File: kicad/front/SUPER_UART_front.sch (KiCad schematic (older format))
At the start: 0 parts

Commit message: Working on schematic
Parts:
- added MECH1: case, dummy, symbol dummy_mech
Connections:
- wire segments 0 -> 58
- no-connect marks 0 -> 4
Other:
- note added: "&"
- note added: "CS"
- note added: "CTS"
- note added: "DTR"
- note added: "FTDI PIN\n\nRxD\nTxD\nCTS\nRTS"
- note added: "FTDI PIN\n\nRxD\nTxD\nRTS"
- note added: "Function\n\nMOSI\nSCK\nCS\nMISO"
- note added: "Function\n\nSDA_OUT\nSCL\nSDA_IN"
- note added: "I2C connections"
- note added: "I2C mode"
- note added: "MISO"
- note added: "MOSI"
- note added: "Opto channel\n\nDTR\nTxD\nCTS"
- note added: "Opto channel\n\nDTR\nTxD\nRTS\nCTS"
- note added: "Output pin\n\nCTS\nTxD\nCTS"
- note added: "Output pin\n\nRxD\nTxD\nRTS\nCTS"
- note added: "RTS"
- note added: "RxD"
- note added: "RxD B\n\nTxD B"
- note added: "RxD C\n\nTxD C"
- note added: "RxD D"
- note added: "RxD D\n\nTxD D"
- note added: "SCK"
- note added: "SCL"
- note added: "SDA"
- note added: "SPI connections"
- note added: "SPI mode"
- note added: "SPY mode"
- note added: "TxD"
- note added: "TxD B"
- note added: "TxD C"
- note added: "TxD D"
- note added: "UART mode"
- note added: "WP"
- note added: "normal mode"

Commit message: Working on schematic
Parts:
- added C1: 10u, niceRLC:0805_N, symbol C
- added CON1: PIN-2x20, PIN-2x20_N, symbol PIN-2x20
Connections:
- net labels added: +5V, CLPD_OE, CPLD_BOOT_EN, CTS_A, CTS_B, CTS_C, CTS_D, DCD_D, DSR_D, DTR_A, DTR_B, DTR_C, DTR_D, EECLK, EECS, EEDATA, FTDI_RESET, GND, RI_D, RTS_D, RXD_A, RXD_B, RXD_C, RXD_D, SR_CLK, SR_DATA, SR_LOAD, TXD_A, TXD_B, TXD_C, TXD_D, ~CTS_A_OC, ~CTS_B_OC, ~PWREN, ~RXD_A_OC, ~RXD_B_OC, ~USB_SUSPEND
- wire segments 58 -> 178
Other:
- moved on the sheet: MECH1

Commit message: PCB placement
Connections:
- wire segments 178 -> 182
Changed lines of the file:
@@
 I2C connections
 $Sheet
-S 7100 850  1500 900
+S 7100 850  1500 1000
 U 5933A622
 F0 "SUPER_UART_front_RS232" 56
@@
 F16 "RXD_D3" I R 8600 1650 56
 F17 "TXD_D" I L 7100 1650 56
+F18 "~VDD1_EN" I R 8600 1750 56
 $EndSheet
 $Sheet
@@
 F4 "RXD_D_LED" I R 10850 3500 56
 F5 "DTR_B" I L 9200 2250 56
-F6 "TXD_D" I L 9200 1900 56
+F6 "TXD_D" I L 9200 1650 56
 F7 "DTR_D1" I L 9200 1150 56
 F8 "RTS_D1" I L 9200 1050 56
@@
 	9200 4550 8600 4550
 Wire Wire Line
-	7000 1900 9200 1900
-Wire Wire Line
 	8600 2800 8700 2800
 Wire Wire Line
-	8700 2800 8700 1900
-Connection ~ 8700 1900
+	8700 2800 8700 1950
+Connection ~ 8700 1950
 Wire Wire Line
 	8600 2900 8800 2900
@@
 	3250 4250 3950 4250
 Wire Wire Line
-	7000 1900 7000 1650
+	7000 1650 7000 1950
 Connection ~ 7000 1650
 Wire Wire Line
@@
 Wire Wire Line
 	2100 5850 2100 5800
+Wire Wire Line
+	7000 1950 9000 1950
+Wire Wire Line
+	9000 1950 9000 1650
+Wire Wire Line
+	9000 1650 9200 1650
+Wire Wire Line
+	8600 1750 8900 1750
+Wire Wire Line
+	8900 1750 8900 3300
+Connection ~ 8900 3300
 $EndSCHEMATC

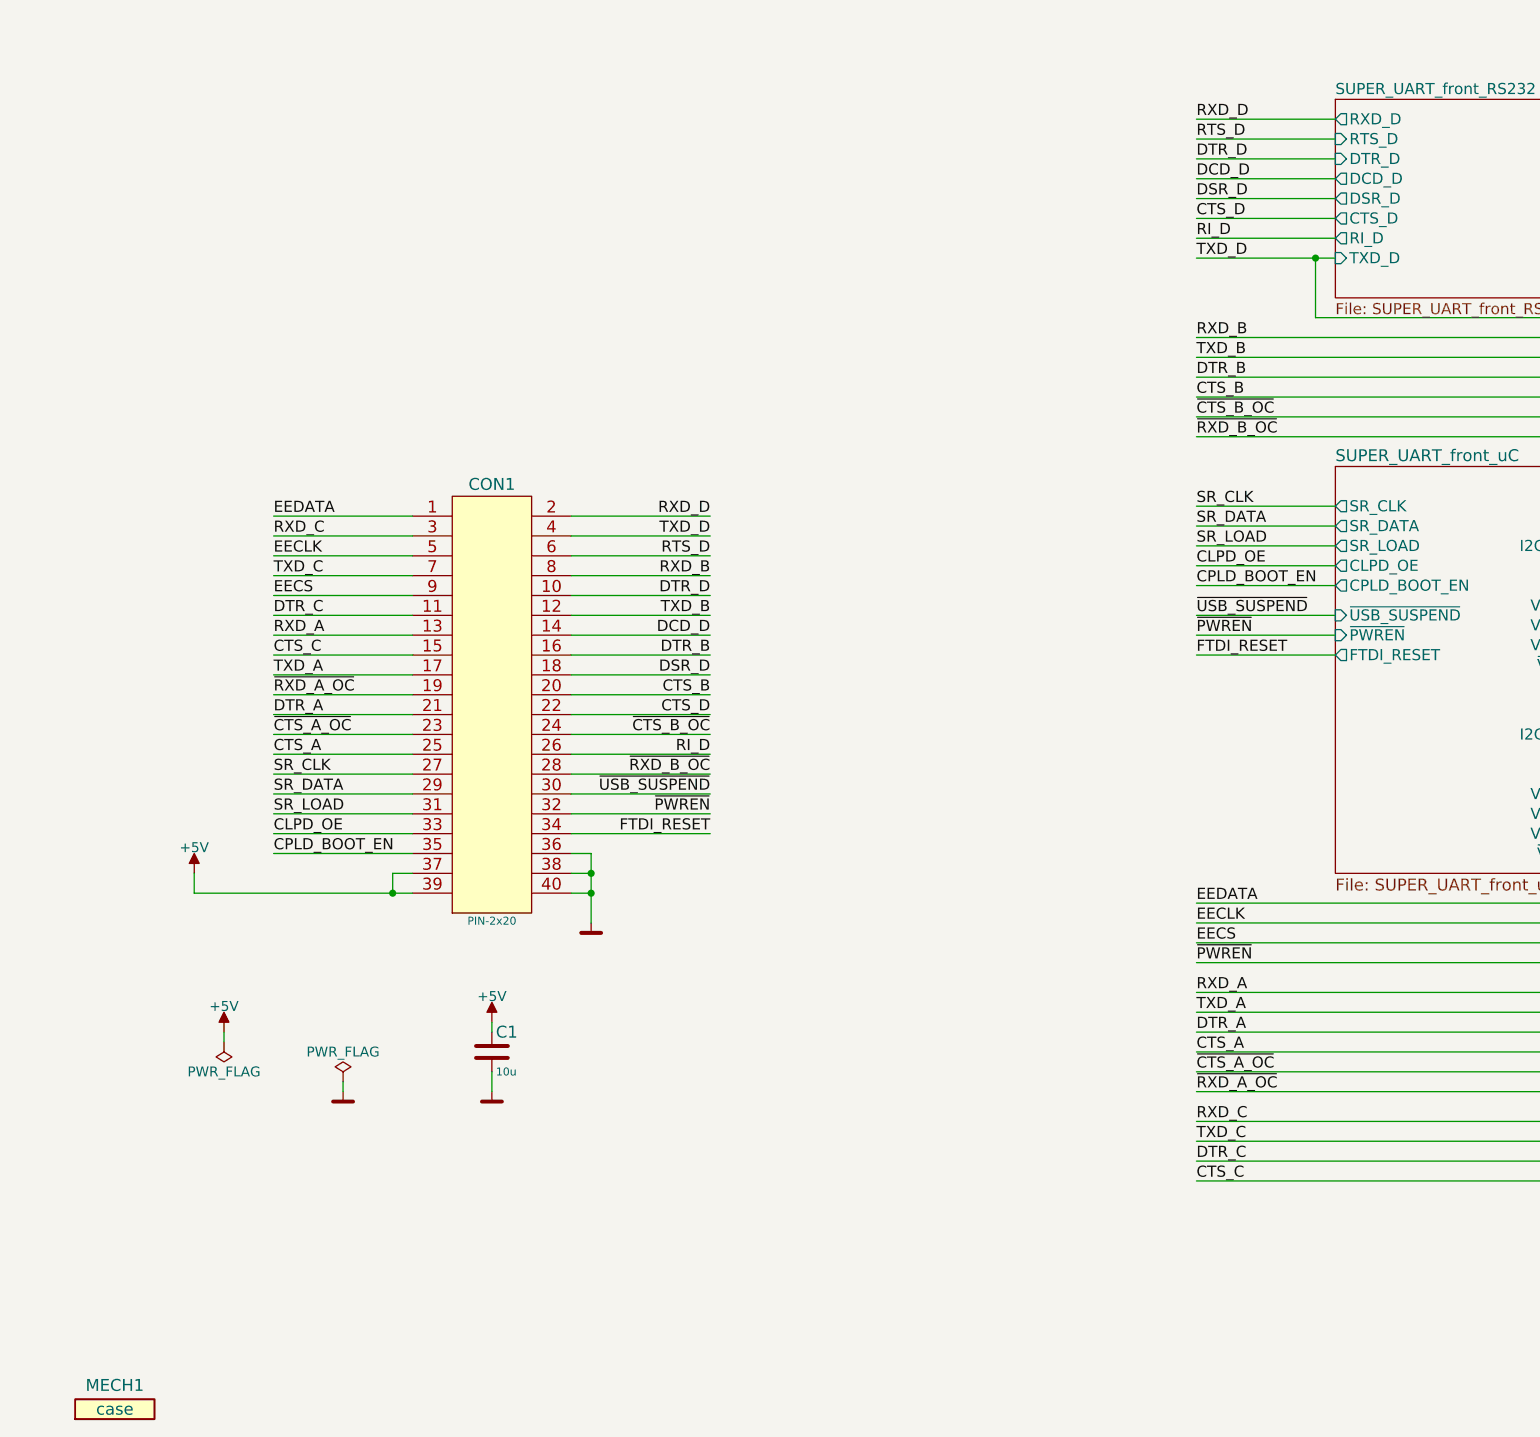
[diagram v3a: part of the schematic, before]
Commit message: Routing before moving to 4 layers
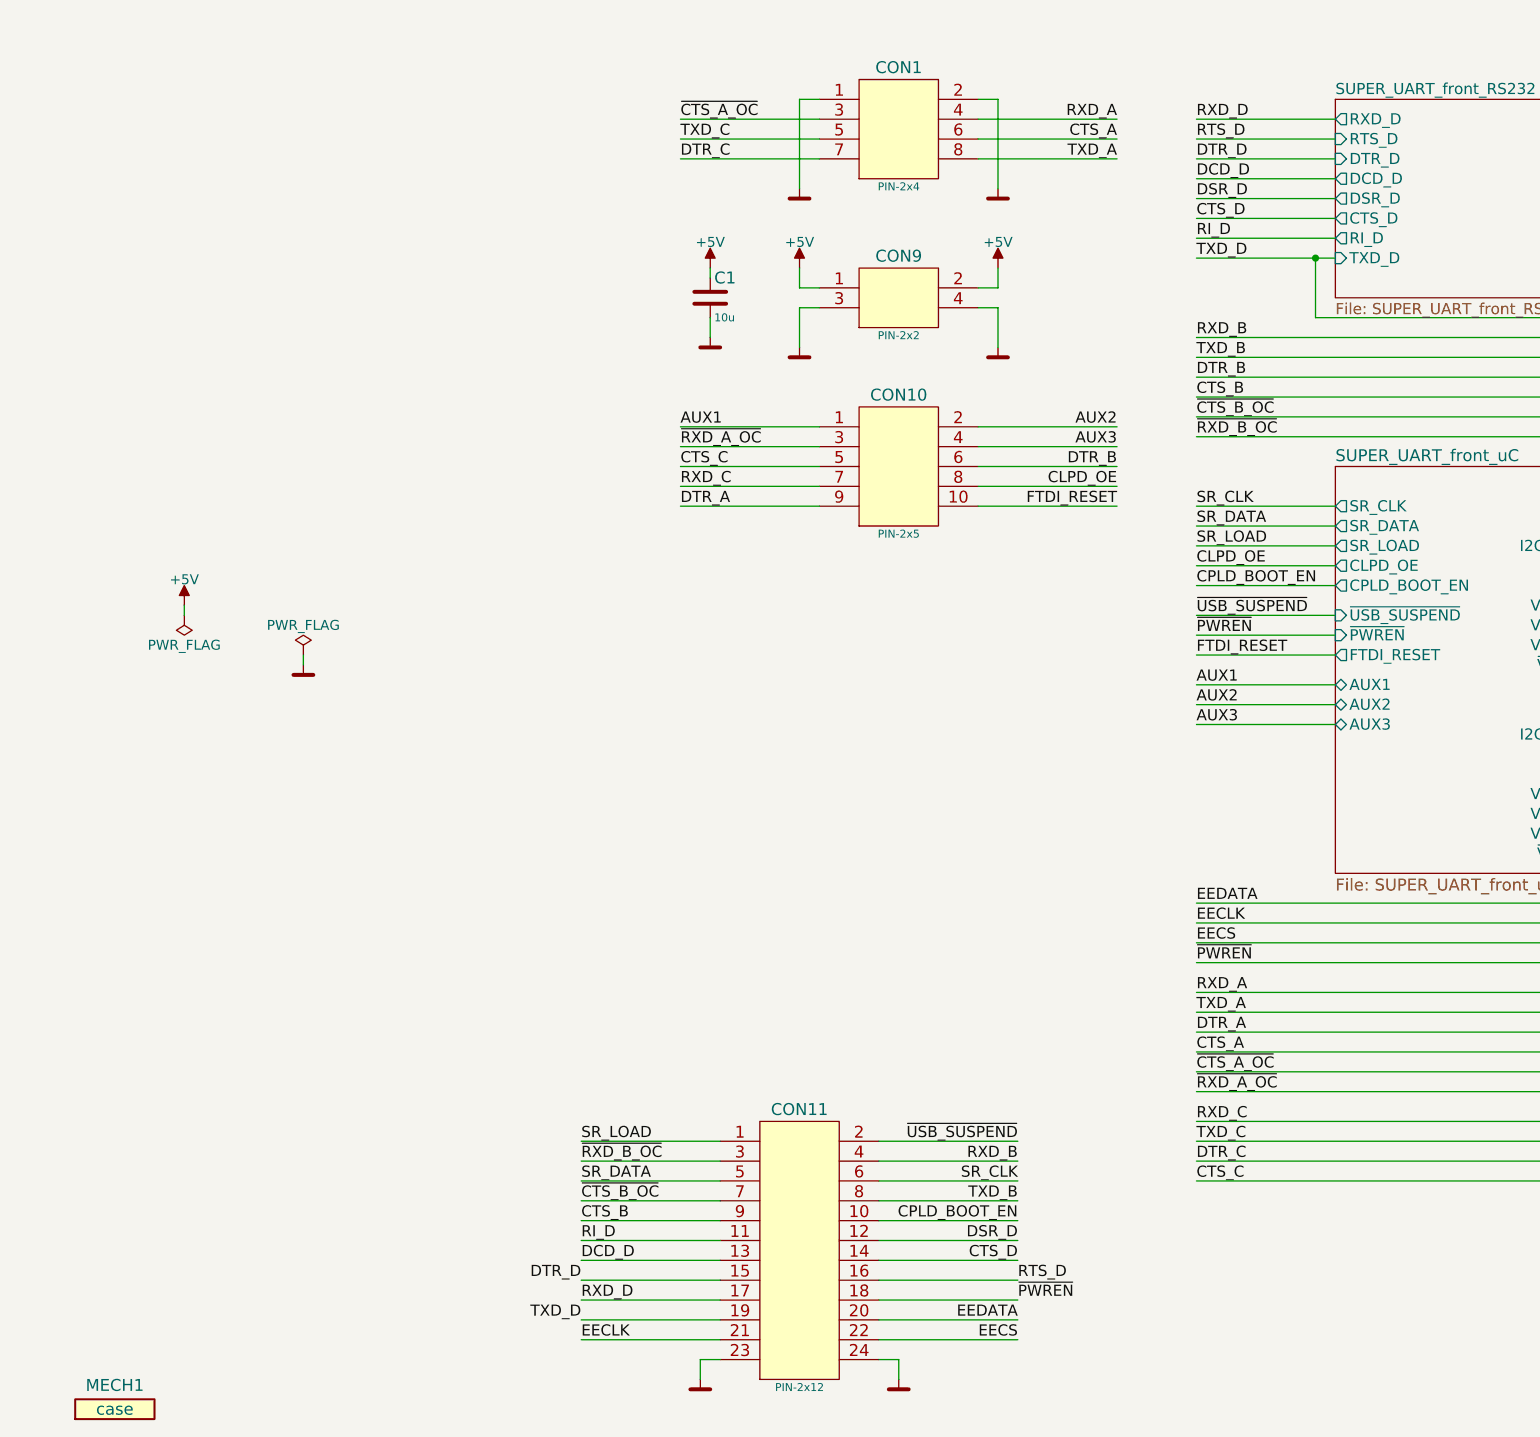
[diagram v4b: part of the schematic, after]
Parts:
- removed CON1: PIN-2x20, PIN-2x20_N, symbol PIN-2x20
- added CON1: PIN-2x4, pnPinheaders:PIN4x2SMD, symbol PIN-2x4
- added CON10: PIN-2x5, pnPinheaders:PIN5x2SMD, symbol PIN-2x5
- added CON11: PIN-2x12, pnPinheaders:PIN12x2SMD, symbol PIN-2x12
- added CON9: PIN-2x2, pnPinheaders:PIN2x2SMD, symbol PIN-2x2
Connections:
- net labels added: AUX1, AUX2, AUX3
- wire segments 182 -> 196
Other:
- moved on the sheet: C1

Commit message: Add missing files
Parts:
- added TP30, TP31, TP32, TP33, TP34, TP35: Testpoint, pnConnector:TP_1mm, symbol Testpoint
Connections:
- net labels added: +3V3, CPLD_OE, VDD1, VDD2
- net labels removed: CLPD_OE
- wire segments 196 -> 153
- no-connect marks 4 -> 0
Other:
- note removed: "&"
- note removed: "CS"
- note removed: "CTS"
- note removed: "DTR"
- note removed: "FTDI PIN\n\nRxD\nTxD\nCTS\nRTS"
- note removed: "FTDI PIN\n\nRxD\nTxD\nRTS"
- note removed: "Function\n\nMOSI\nSCK\nCS\nMISO"
- note removed: "Function\n\nSDA_OUT\nSCL\nSDA_IN"
- note removed: "I2C connections"
- note removed: "I2C mode"
- note removed: "MISO"
- note removed: "MOSI"
- note removed: "Opto channel\n\nDTR\nTxD\nCTS"
- note removed: "Opto channel\n\nDTR\nTxD\nRTS\nCTS"
- note removed: "Output pin\n\nCTS\nTxD\nCTS"
- note removed: "Output pin\n\nRxD\nTxD\nRTS\nCTS"
- note removed: "RTS"
- note removed: "RxD"
- note removed: "RxD B\n\nTxD B"
- note removed: "RxD C\n\nTxD C"
- note removed: "RxD D"
- note removed: "RxD D\n\nTxD D"
- note removed: "SCK"
- note removed: "SCL"
- note removed: "SDA"
- note removed: "SPI connections"
- note removed: "SPI mode"
- note removed: "SPY mode"
- note removed: "TxD"
- note removed: "TxD B"
- note removed: "TxD C"
- note removed: "TxD D"
- note removed: "UART mode"
- note removed: "WP"
- note removed: "normal mode"
- moved on the sheet: C1, CON1, CON10, CON11, CON9, MECH1
